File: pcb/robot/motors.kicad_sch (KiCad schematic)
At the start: 27 parts, among them J3 Conn_01x06_MountingPin, J5 Conn_01x06_MountingPin, J6 MotorCable, J7 MotorCable, Q6 SN74AHC125RGYR, U8 DRV8830DRCR, U9 DRV8830DRCR

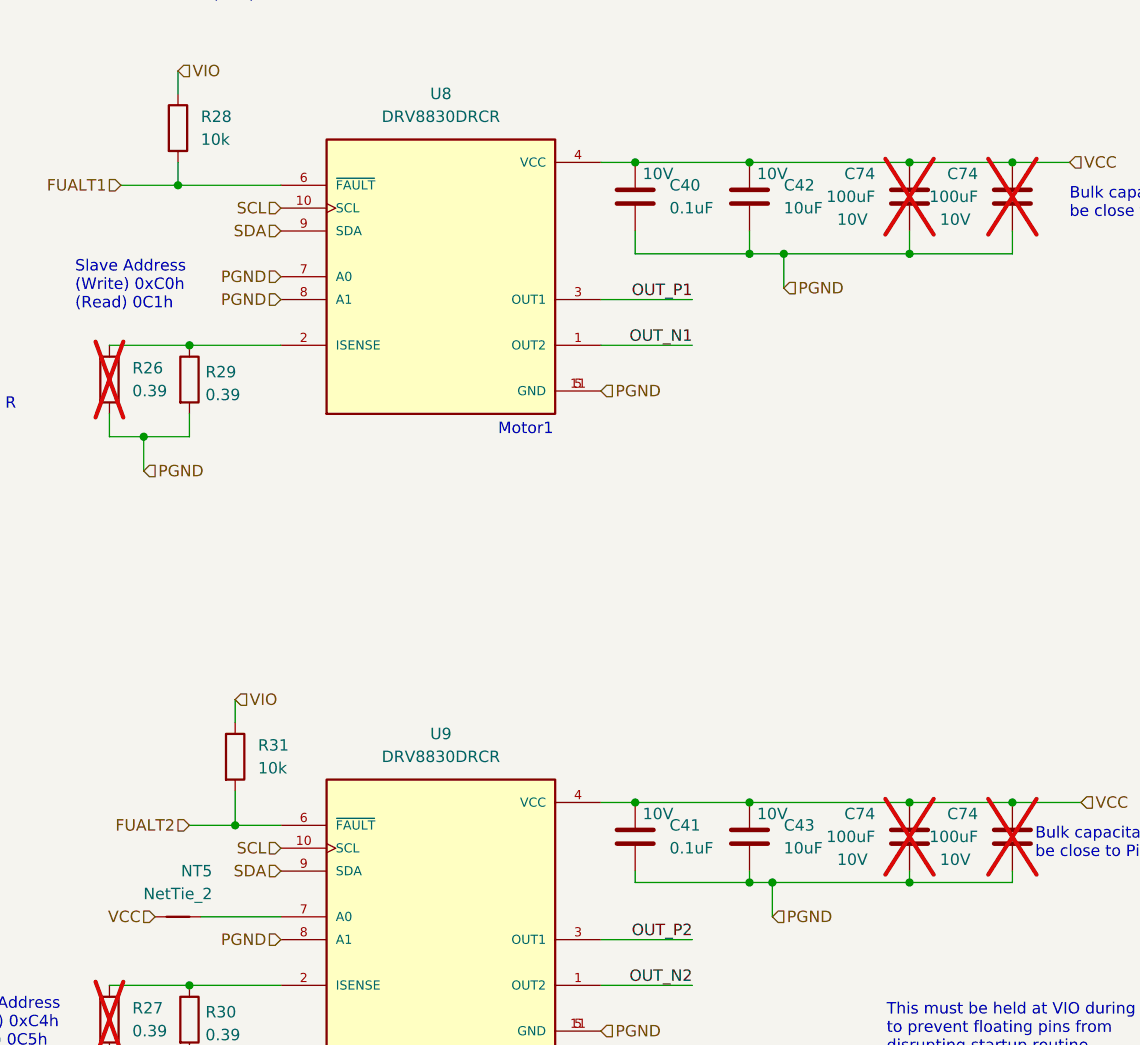
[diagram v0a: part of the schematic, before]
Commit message: Modularized usb-pd board and main board split
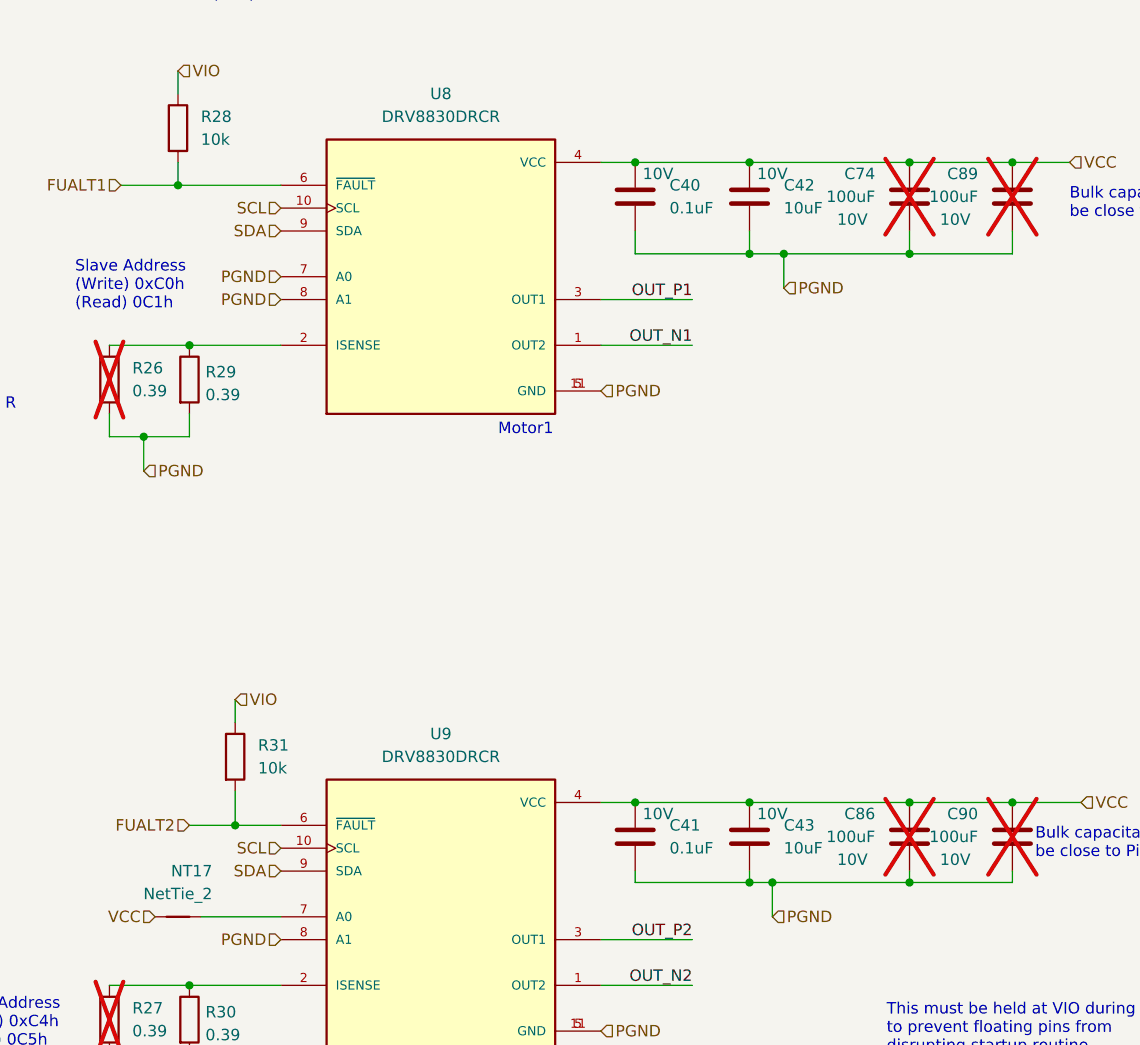
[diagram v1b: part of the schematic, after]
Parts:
- renumbered C74 to C86, C74 to C89, C74 to C90, NT5 to NT17

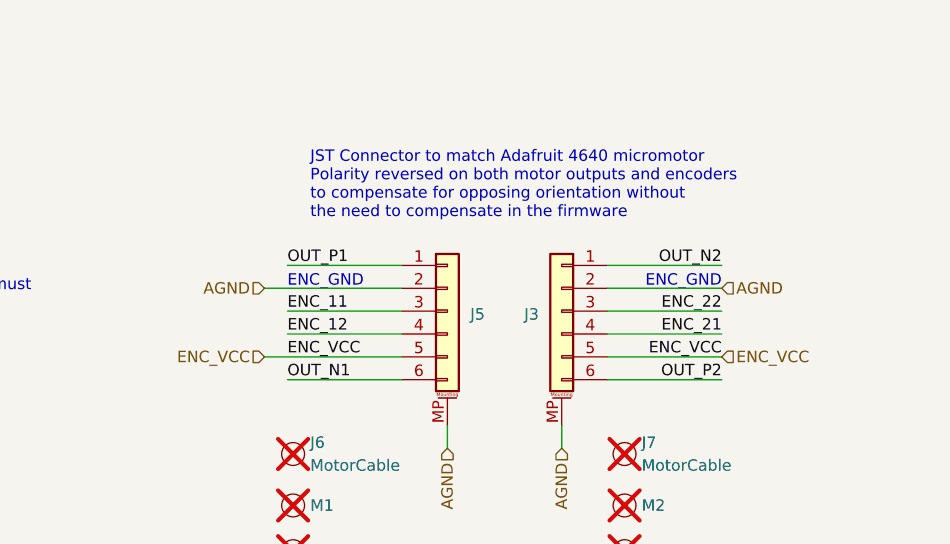
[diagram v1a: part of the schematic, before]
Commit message: Fix reversed motor connector pins on J3/J5 (fixes #15)
Swap pins 1/6 (motor phase polarity) and 2/5 (encoder VCC/GND) on
both motor JST connectors (J3, J5), so standard JST cables work
without custom re-pinning and without needing a software-side
forward/backward negation workaround. Pins 3/4 (encoder A/B) left
untouched. PCB copper re-routed to match; verified 0 unconnected
items via DRC and no new ERC violations on J3/J5.

Firmware's negation workaround should be removed once this hardware
revision is in use, or the two corrections will cancel out.

Fix leftover note typo and grid nudge (follow-up to #3)

Correct CC jumper note in USB_PD_Module.kicad_sch to reference the
actual R3/R4 designators used, and nudge SW1 onto grid in
Protection.kicad_sch. No net changes.
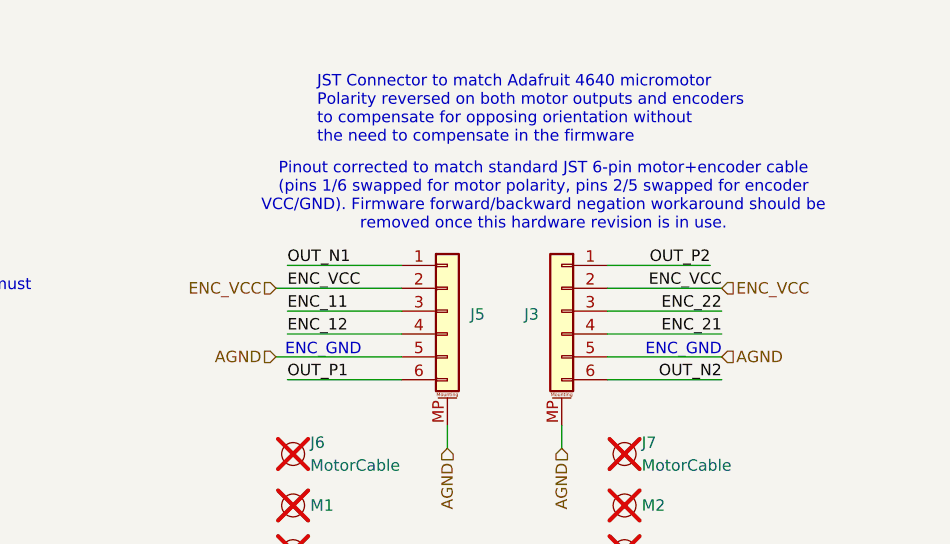
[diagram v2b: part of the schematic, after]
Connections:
- net AGND: now also J3.5 (Pin_5), J5.5 (Pin_5); no longer J3.2 (Pin_2), J5.2 (Pin_2)
- net ENC_VCC: now also J3.2 (Pin_2), J5.2 (Pin_2); no longer J3.5 (Pin_5), J5.5 (Pin_5)
- net OUT_N1: now also J5.1 (Pin_1); no longer J5.6 (Pin_6)
- net OUT_N2: now also J3.6 (Pin_6); no longer J3.1 (Pin_1)
- net OUT_P1: now also J5.6 (Pin_6); no longer J5.1 (Pin_1)
- net OUT_P2: now also J3.1 (Pin_1); no longer J3.6 (Pin_6)
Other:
- note added: "Pinout corrected to match standard JST 6-pin motor+encoder cable (pins 1/6 swapped for motor polarity, pins 2/5 swapped for encoder VCC/GND). Firmware forward/backward negation workaround should be removed once this hardware revision is in use."

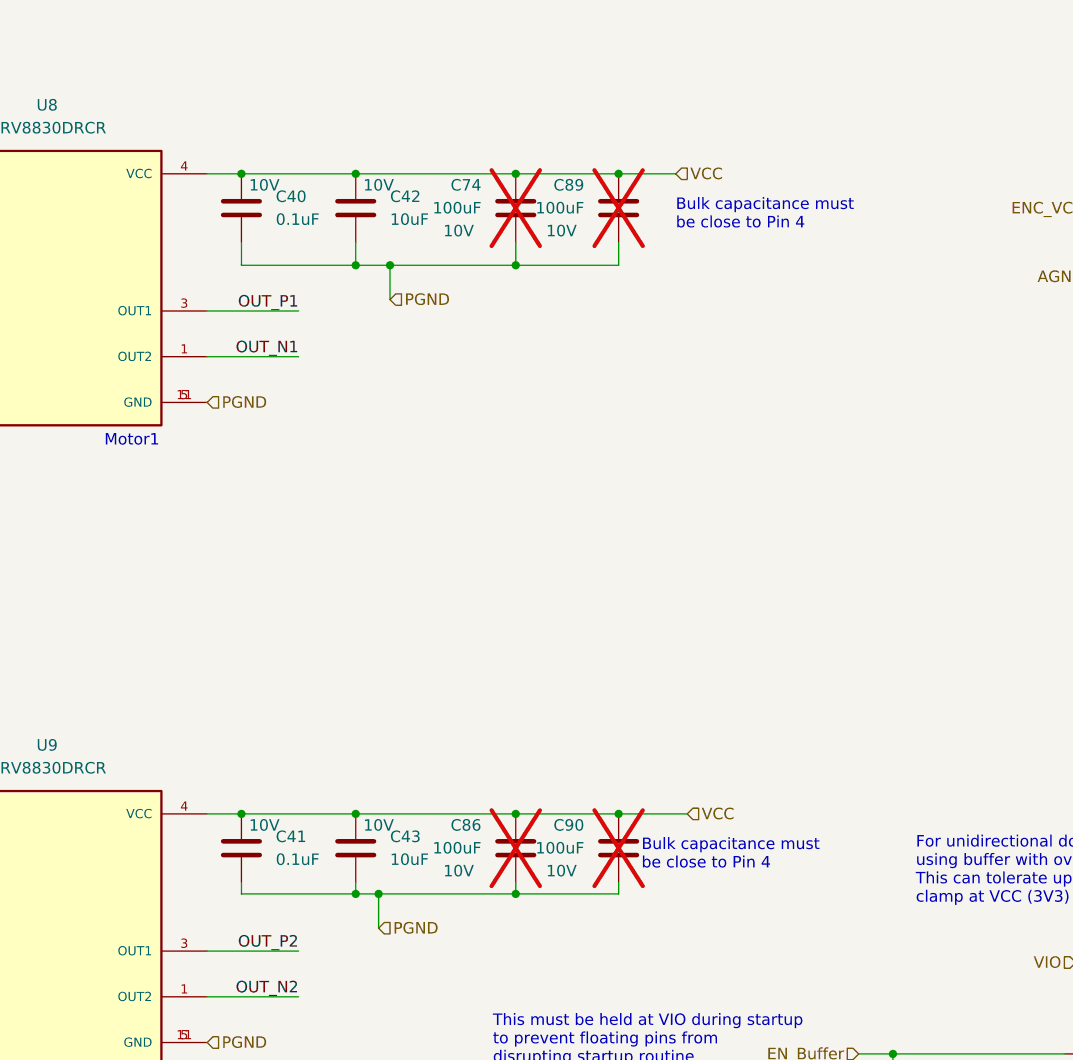
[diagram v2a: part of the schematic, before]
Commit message: Remove unnecessary bulk caps C74/C86/C89/C90 (fixes #16)
Delete the 4 redundant 100uF bulk caps (VCC-GND, motor driver rail)
from both schematic and PCB to reclaim board space. Stress testing
(see #4 discussion) showed rail variation stays under 100mV even
without them, so the extra bulk capacitance added after the earlier
UVLO investigation is no longer needed.

Verified via ERC/DRC: same violation counts as before (314/7),
0 unconnected items - no regressions from the removal.
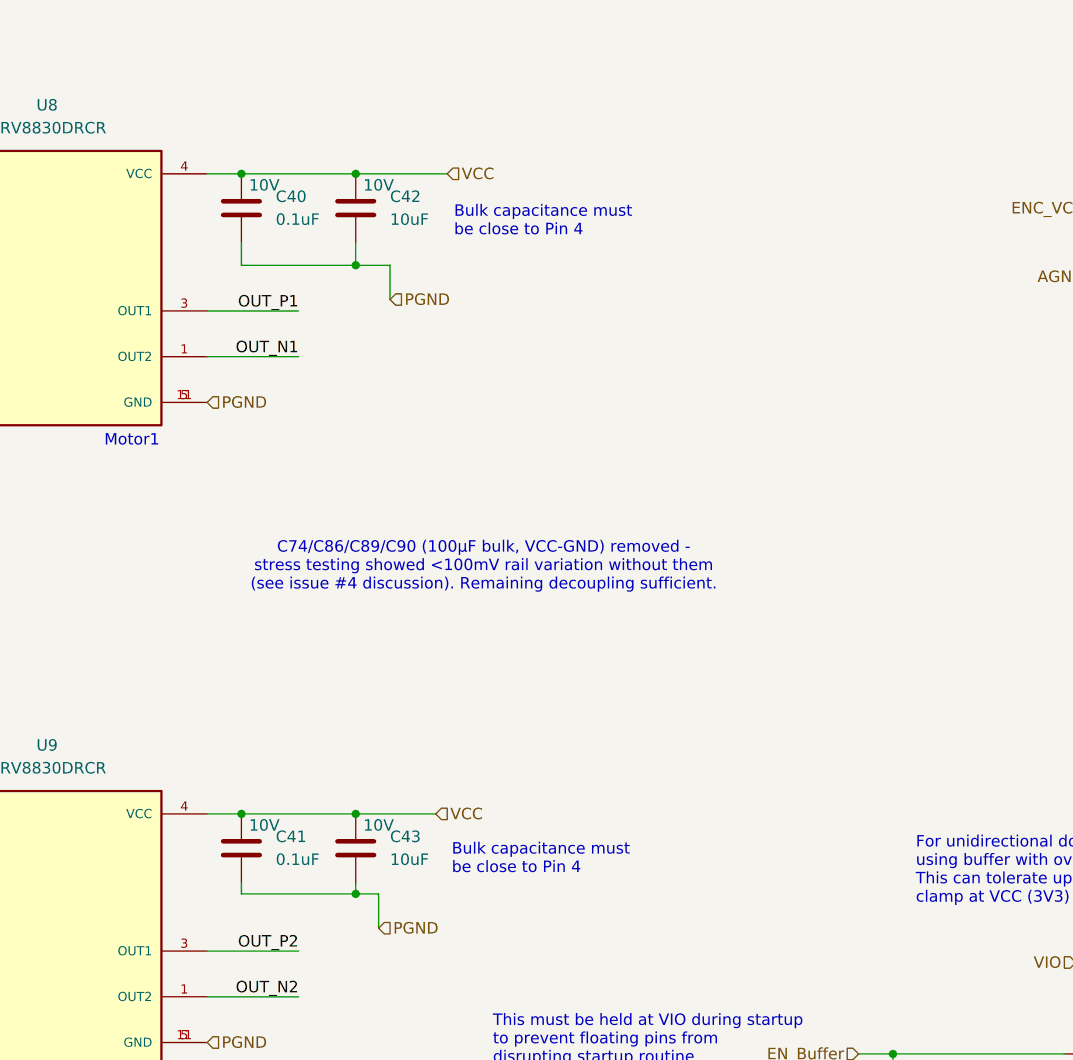
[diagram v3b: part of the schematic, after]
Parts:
- removed C74, C86, C89, C90: 100uF, robot:CP_Elec_APXJ100ARA271MF61G, symbol robot:C
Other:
- note added: "C74/C86/C89/C90 (100µF bulk, VCC-GND) removed - stress testing showed <100mV rail variation without them (see issue #4 discussion). Remaining decoupling sufficient."
